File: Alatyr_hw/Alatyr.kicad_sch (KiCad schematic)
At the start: 64 parts, among them M1 Vibro_10mm, SW1 IT1198, SW2 IT1198, U1 JDY-23, U2 LSM6DS3

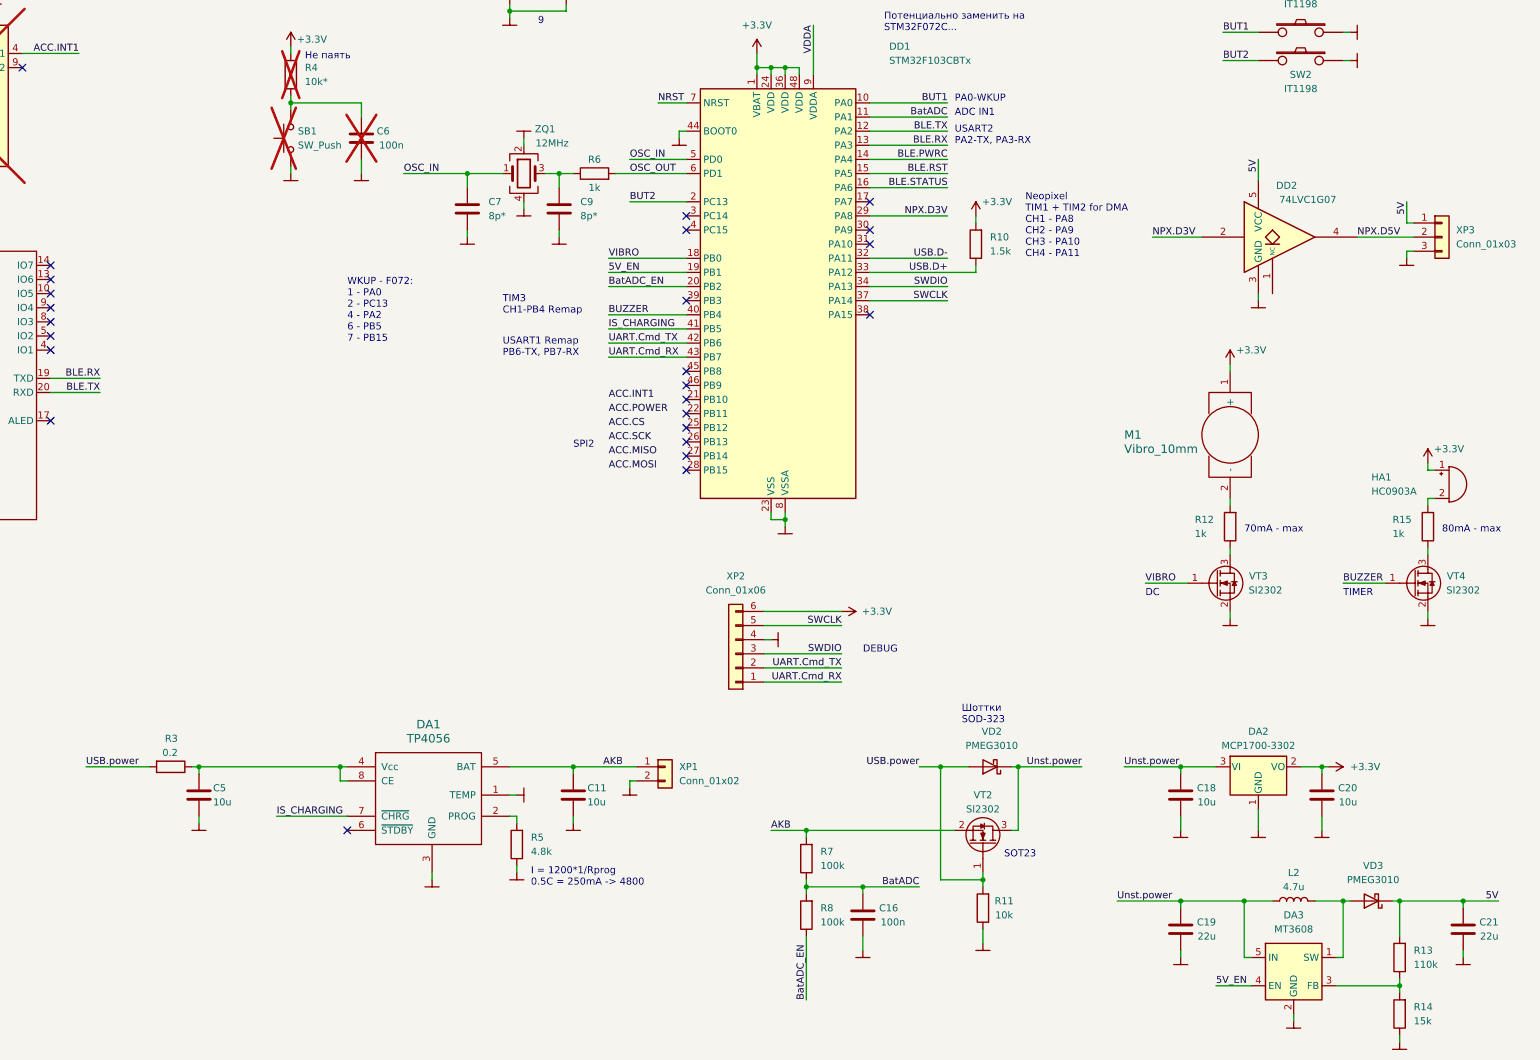
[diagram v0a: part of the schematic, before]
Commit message: PCB wired, small cover fixes
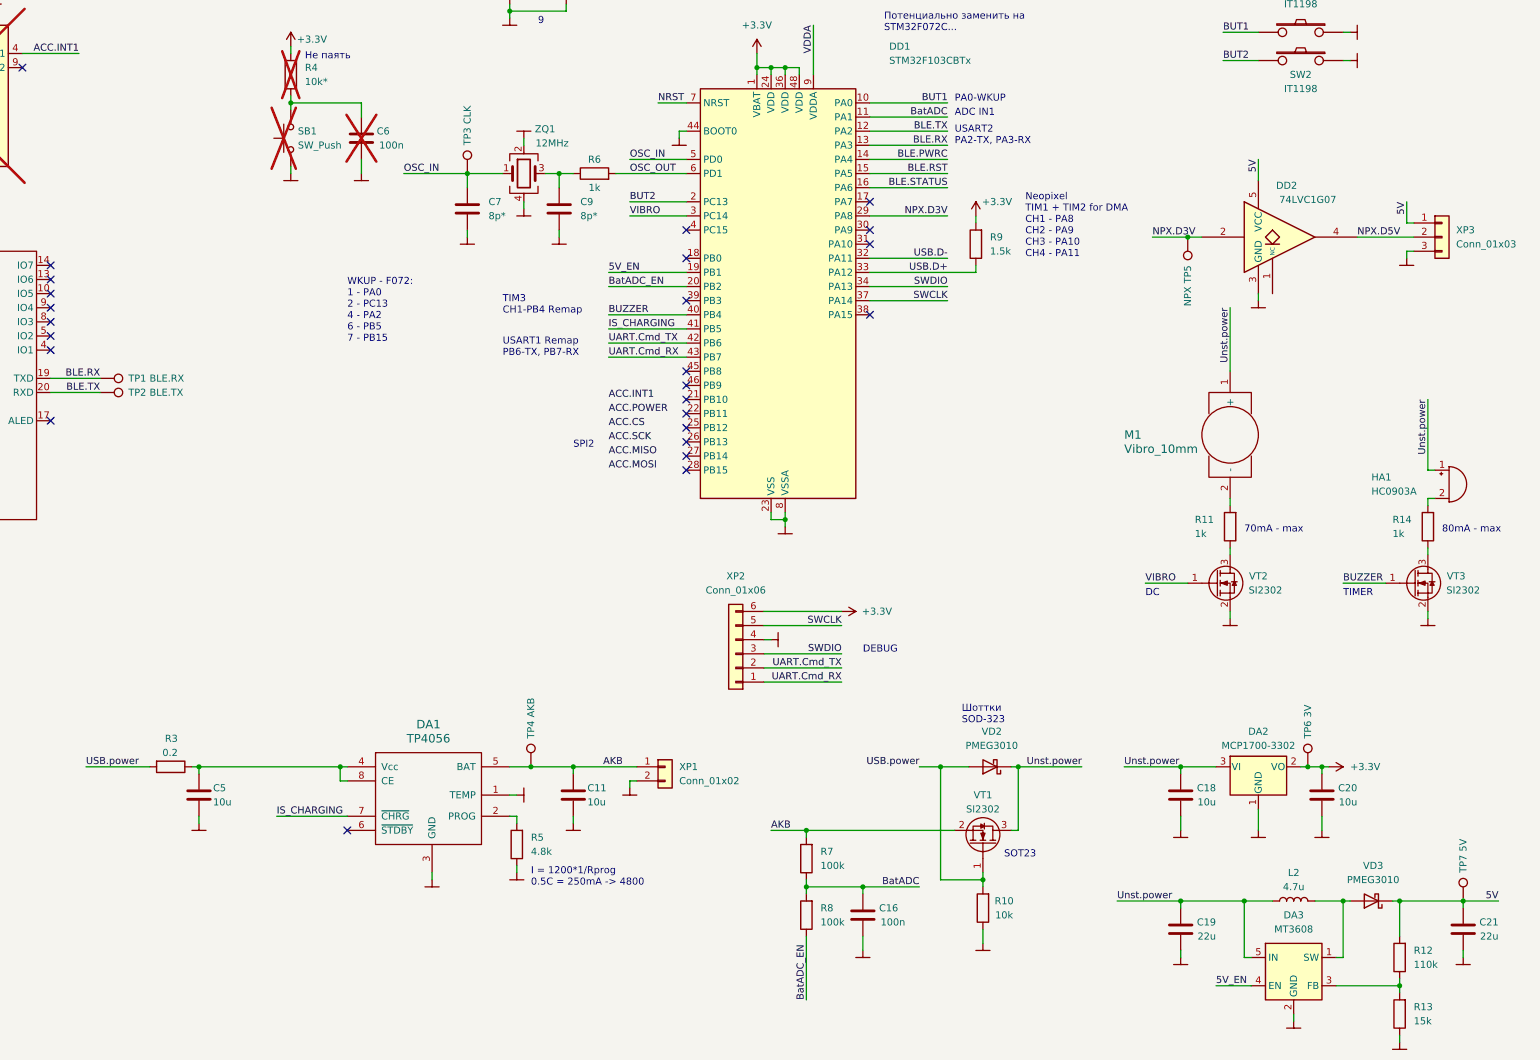
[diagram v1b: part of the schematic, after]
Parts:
- added TP1: BLE.RX, TestPoint:TestPoint_Pad_D1.0mm, symbol Connector:TestPoint
- added TP2: BLE.TX, TestPoint:TestPoint_Pad_D1.0mm, symbol Connector:TestPoint
- added TP3: CLK, TestPoint:TestPoint_Pad_D1.0mm, symbol Connector:TestPoint
- added TP4: AKB, TestPoint:TestPoint_Pad_D1.0mm, symbol Connector:TestPoint
- added TP5: NPX, TestPoint:TestPoint_Pad_D1.0mm, symbol Connector:TestPoint
- added TP6: 3V, TestPoint:TestPoint_Pad_D1.0mm, symbol Connector:TestPoint
- added TP7: 5V, TestPoint:TestPoint_Pad_D1.0mm, symbol Connector:TestPoint
- renumbered R11 to R10, R12 to R11, R13 to R12, R14 to R13, R15 to R14, R10 to R9, VT2 to VT1, VT3 to VT2, VT4 to VT3
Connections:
- net +3V3: now also TP6.1; no longer HA1.1 (-), M1.1 (+)
- net 5V: now also TP7.1
- net AKB: now also TP4.1
- net BLE.RX: now also TP1.1
- net BLE.TX: now also TP2.1
- net NPX.D3V: now also TP5.1
- net OSC_IN: now also TP3.1
- net Unst.power: now also HA1.1 (-), M1.1 (+)
- net VIBRO: now also DD1.3 (PC14); no longer DD1.18 (PB0)

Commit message: Start writing firmware
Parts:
- H1, H2, H3: footprint Kais_Lib:Hole_2.4 -> MountingHole:MountingHole_2.5mm
- XP1: footprint Connector_PinHeader_2.54mm:PinHeader_1x02_P2.54mm_Horizontal -> Connector_PinHeader_2.54mm:PinHeader_1x02_P2.54mm_Vertical
- XP2: footprint Connector_PinHeader_2.54mm:PinHeader_1x06_P2.54mm_Horizontal -> Connector_PinHeader_2.54mm:PinHeader_1x06_P2.54mm_Vertical
- XP3: footprint Connector_PinHeader_2.54mm:PinHeader_1x03_P2.54mm_Horizontal -> Connector_PinHeader_2.54mm:PinHeader_1x03_P2.54mm_Vertical
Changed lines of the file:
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@@
       (effects (font (size 1.27 1.27)) (justify left))
     )
-    (property "Footprint" "Kais_Lib:Hole_2.4" (at 313.69 33.02 0)
+    (property "Footprint" "MountingHole:MountingHole_2.5mm" (at 313.69 33.02 0)
       (effects (font (size 1.27 1.27)) hide)
     )
@@
       (effects (font (size 1.27 1.27)) (justify left))
     )
-    (property "Footprint" "Connector_PinHeader_2.54mm:PinHeader_1x02_P2.54mm_Horizontal" (at 248.92 189.23 0)
+    (property "Footprint" "Connector_PinHeader_2.54mm:PinHeader_1x02_P2.54mm_Vertical" (at 248.92 189.23 0)
       (effects (font (size 1.27 1.27)) hide)
     )
@@
       (effects (font (size 1.27 1.27)) (justify left))
     )
-    (property "Footprint" "Connector_PinHeader_2.54mm:PinHeader_1x03_P2.54mm_Horizontal" (at 388.62 93.98 0)
+    (property "Footprint" "Connector_PinHeader_2.54mm:PinHeader_1x03_P2.54mm_Vertical" (at 388.62 93.98 0)
       (effects (font (size 1.27 1.27)) hide)
     )
@@
       (effects (font (size 1.27 1.27)))
     )
-    (property "Footprint" "Connector_PinHeader_2.54mm:PinHeader_1x06_P2.54mm_Horizontal" (at 261.62 168.91 0)
+    (property "Footprint" "Connector_PinHeader_2.54mm:PinHeader_1x06_P2.54mm_Vertical" (at 261.62 168.91 0)
       (effects (font (size 1.27 1.27)) hide)
     )
@@
       (effects (font (size 1.27 1.27)) (justify left))
     )
-    (property "Footprint" "Kais_Lib:Hole_2.4" (at 313.69 27.94 0)
+    (property "Footprint" "MountingHole:MountingHole_2.5mm" (at 313.69 27.94 0)
       (effects (font (size 1.27 1.27)) hide)
     )
@@
       (effects (font (size 1.27 1.27)) (justify left))
     )
-    (property "Footprint" "Kais_Lib:Hole_2.4" (at 313.69 22.86 0)
-      (effects (font (size 1.27 1.27)) hide)
-    )
+    (property "Footprint" "MountingHole:MountingHole_2.5mm" (at 313.69 22.86 0)
+      (effects (font (size 1.27 1.27)) hide)
+    )
